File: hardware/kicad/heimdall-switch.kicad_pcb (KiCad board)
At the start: 2 copper layers, 63.5 x 23 mm, 42 parts, among them J1 TC2030-NL (SWD), J2 LOAD_OUT, J3 BATT_IN, J4 B3B-XH-A, Q1 AO3400A, Q2 BSS84, Q3 AO4407A, Q4 AO4407A, Q5 AO3400A, Q6 BSS84, SW1 PTS810, U1 BT832, U2 TPS629206, Y1 32.768kHz

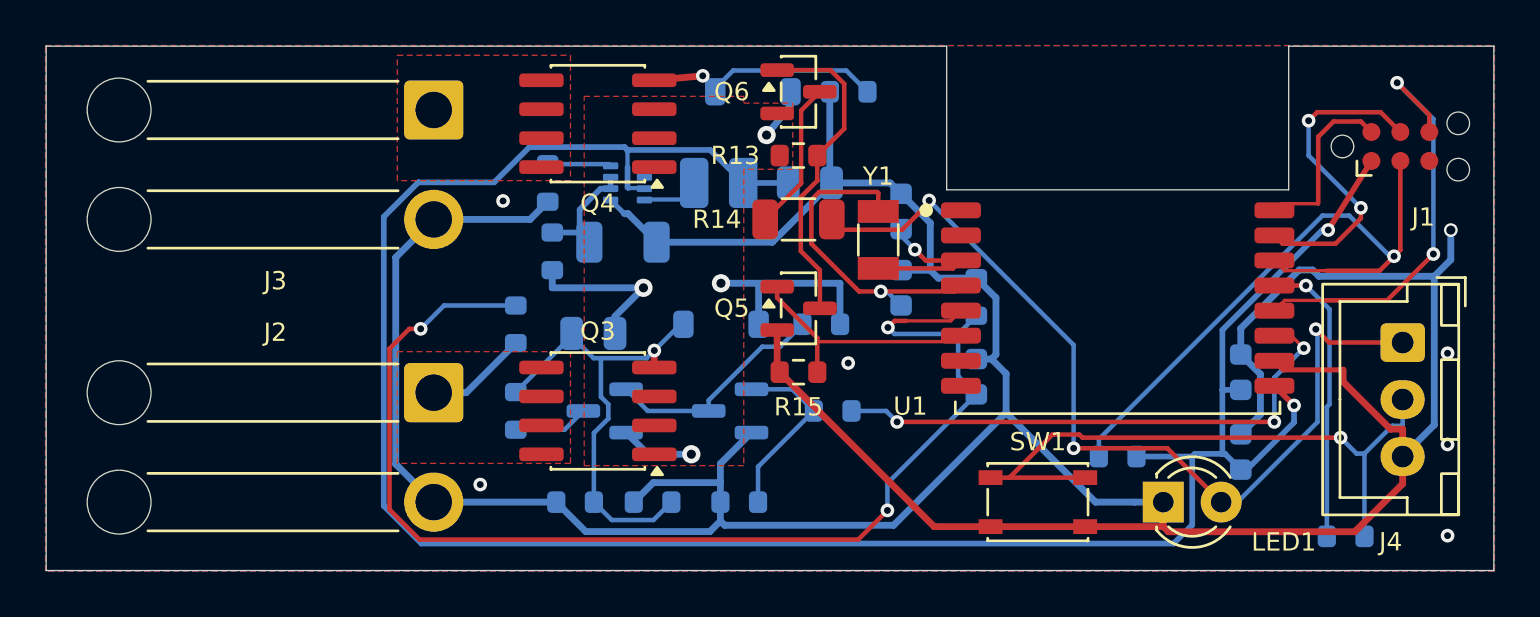
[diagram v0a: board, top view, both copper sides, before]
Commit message: Revert "J1: Tag-Connect TC2030-NL in place of the 2x5 SWD header"
This reverts commit dd4bac91d17cbcc49fd8600aaa5e4591b524028c.
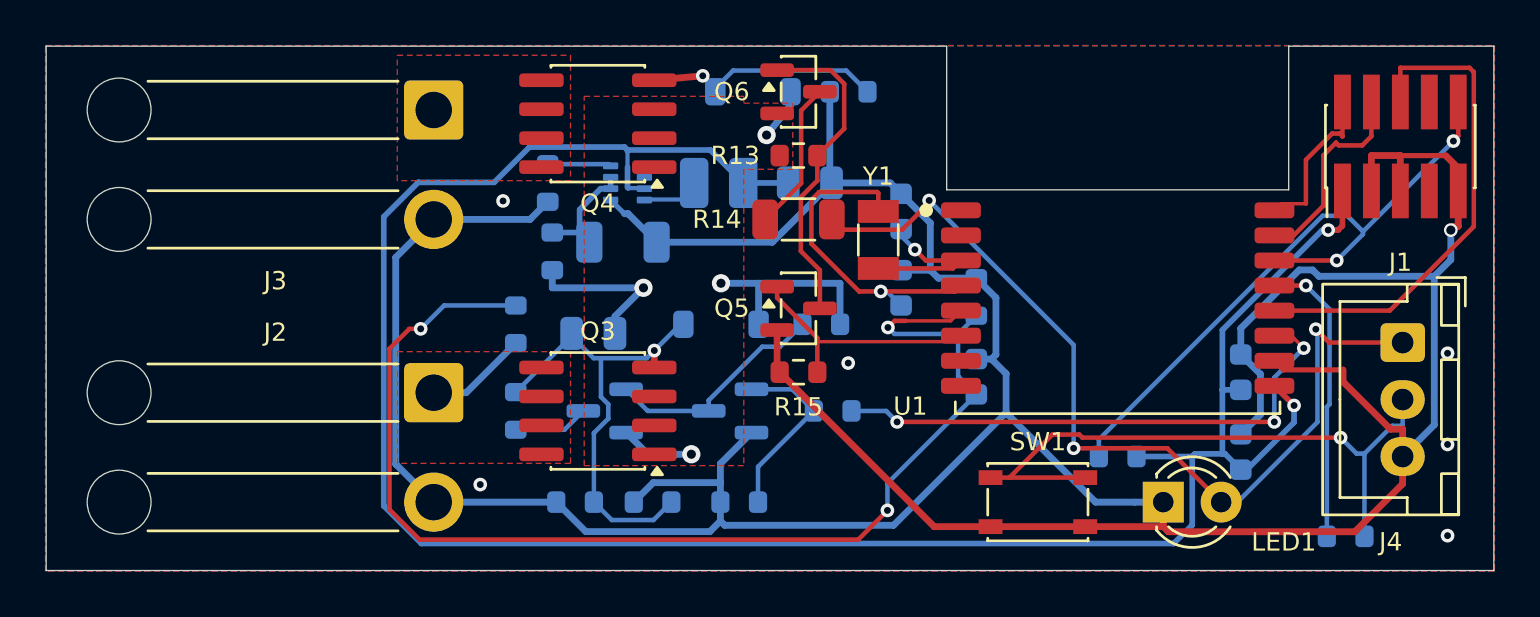
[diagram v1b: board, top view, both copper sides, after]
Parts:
- J1: value TC2030-NL (SWD) -> SWD (ARM 10-pin); footprint Connector:Tag-Connect_TC2030-IDC-NL_2x03_P1.27mm_Vertical -> Connector_PinHeader_1.27mm:PinHeader_2x05_P1.27mm_Vertical_SMD
- turned J1 to 90 degrees
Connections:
- J1 pad 3: /nRESET -> GND
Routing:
- net GND: track 167.1 -> 177.1 mm
- net /SWDCLK: track 14.2 -> 8.95 mm, vias 2 -> 0
- net /SWO: track 18.9 -> 21.9 mm, vias 2 -> 0
- net +3V3: track 100.6 -> 99.2 mm
- net /SWDIO: track 7.78 -> 7.06 mm
- net /nRESET: track 28.5 -> 28.6 mm, vias 1 -> 2
